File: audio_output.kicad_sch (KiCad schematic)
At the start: 33 parts, among them J10 NCJ6FA-H-0, J9 NCJ6FA-H-0, U5 OPA1656ID, U6 THAT1646, U7 THAT1646

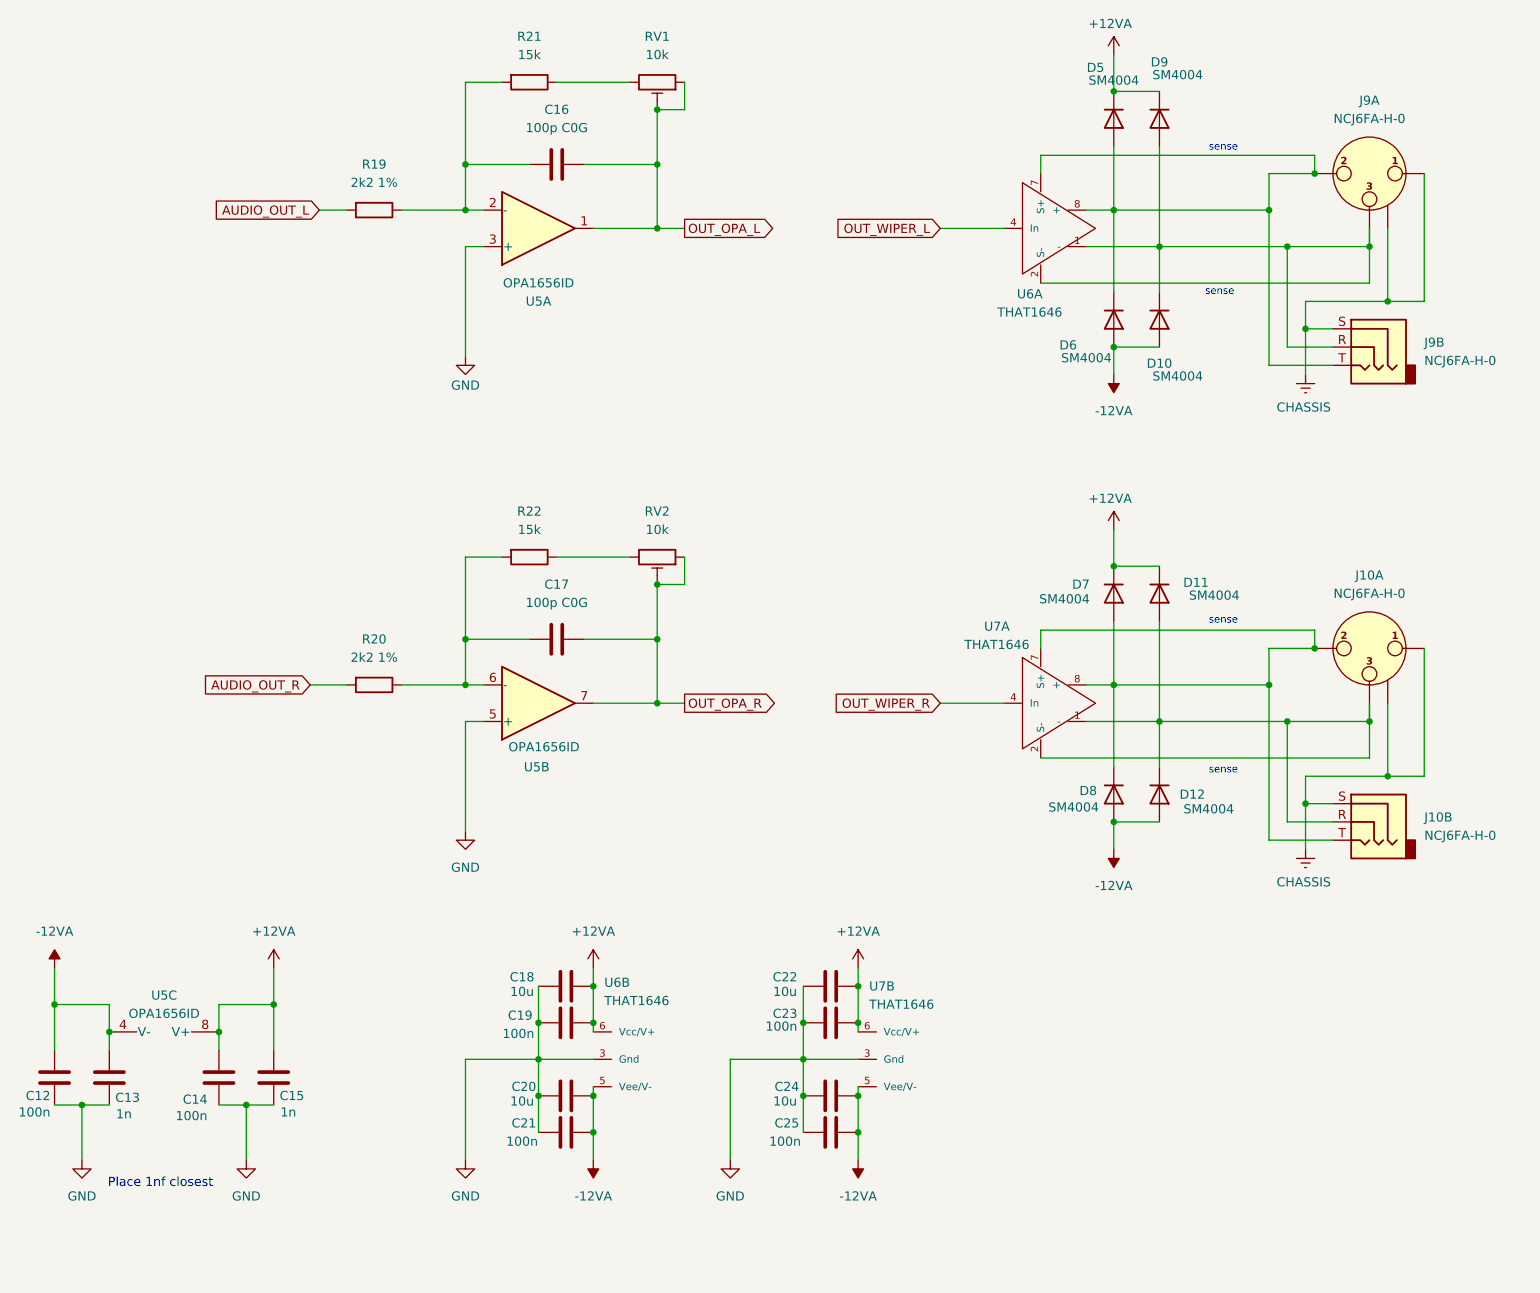
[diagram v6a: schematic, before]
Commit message: change docs to use RS3-1212D
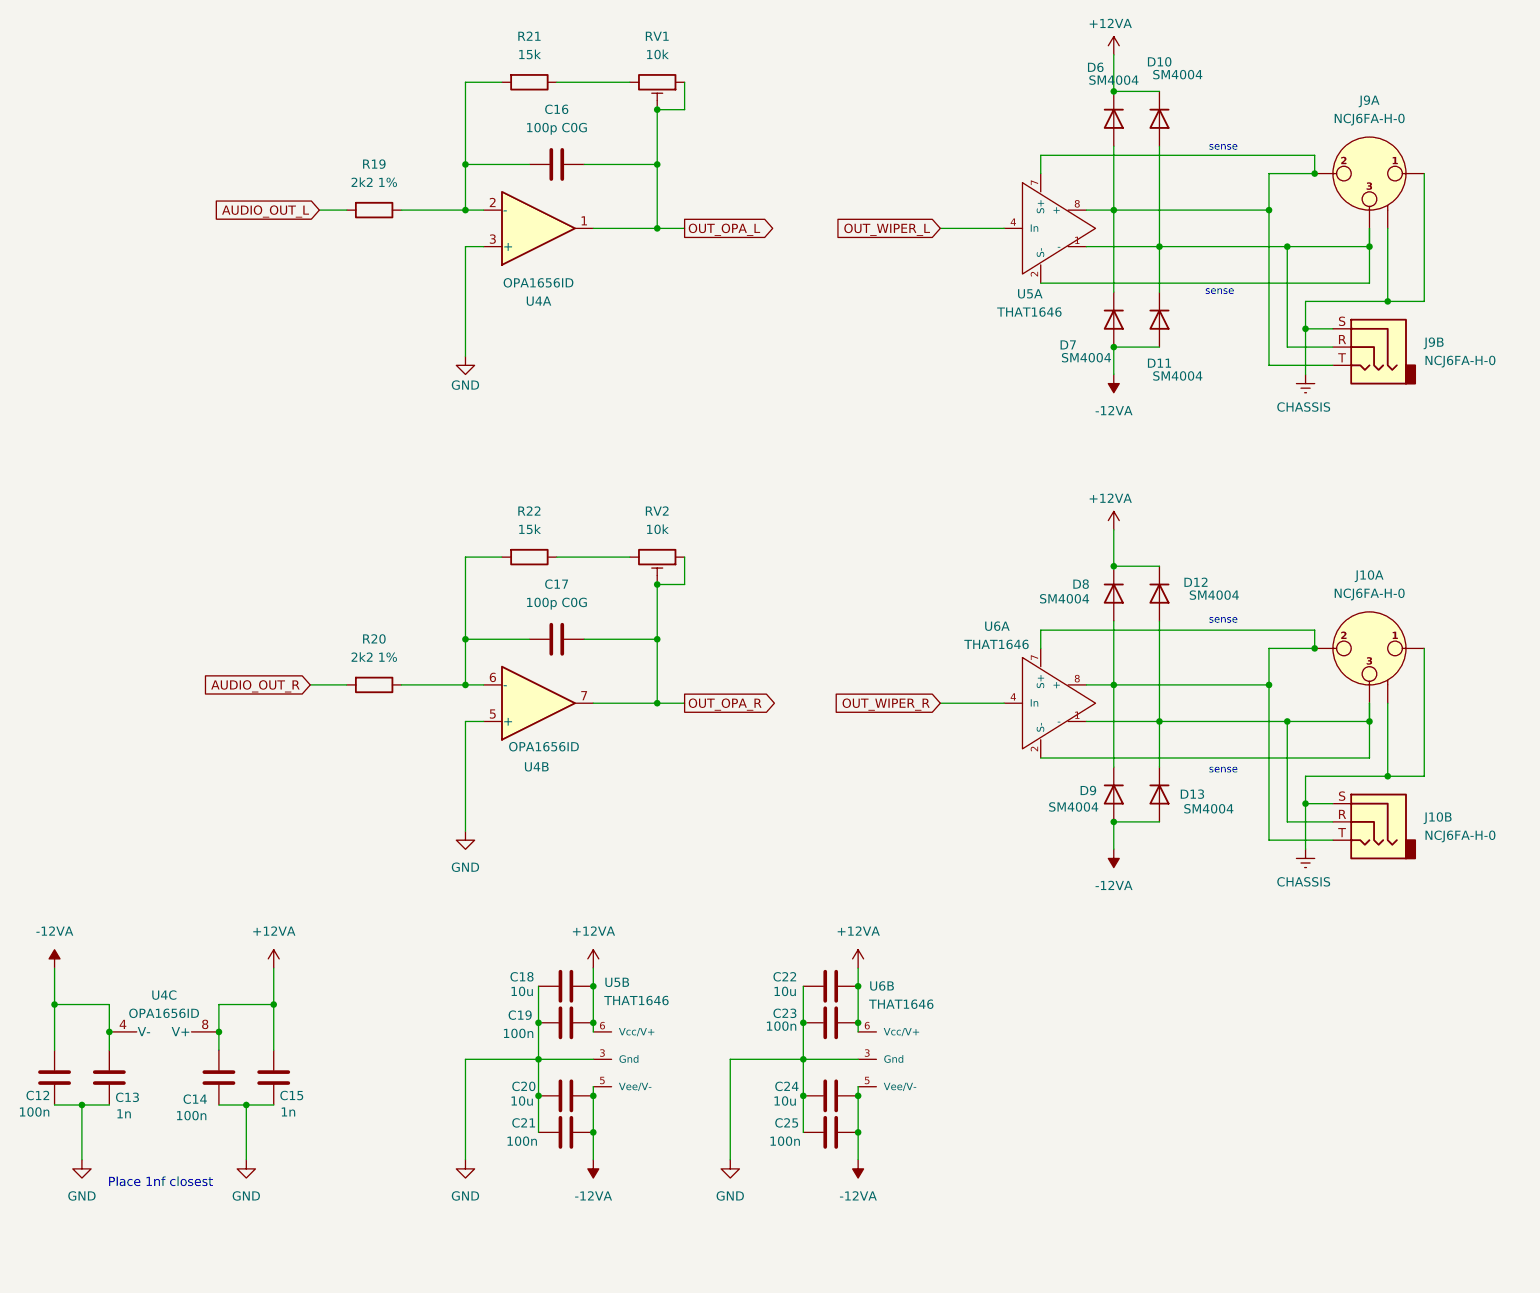
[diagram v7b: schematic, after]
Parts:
- renumbered D9 to D10, D10 to D11, D11 to D12, D12 to D13, D5 to D6, D6 to D7, D7 to D8, D8 to D9, U5 to U4, U6 to U5, U7 to U6
